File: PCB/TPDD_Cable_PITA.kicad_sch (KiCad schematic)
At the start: 5 parts

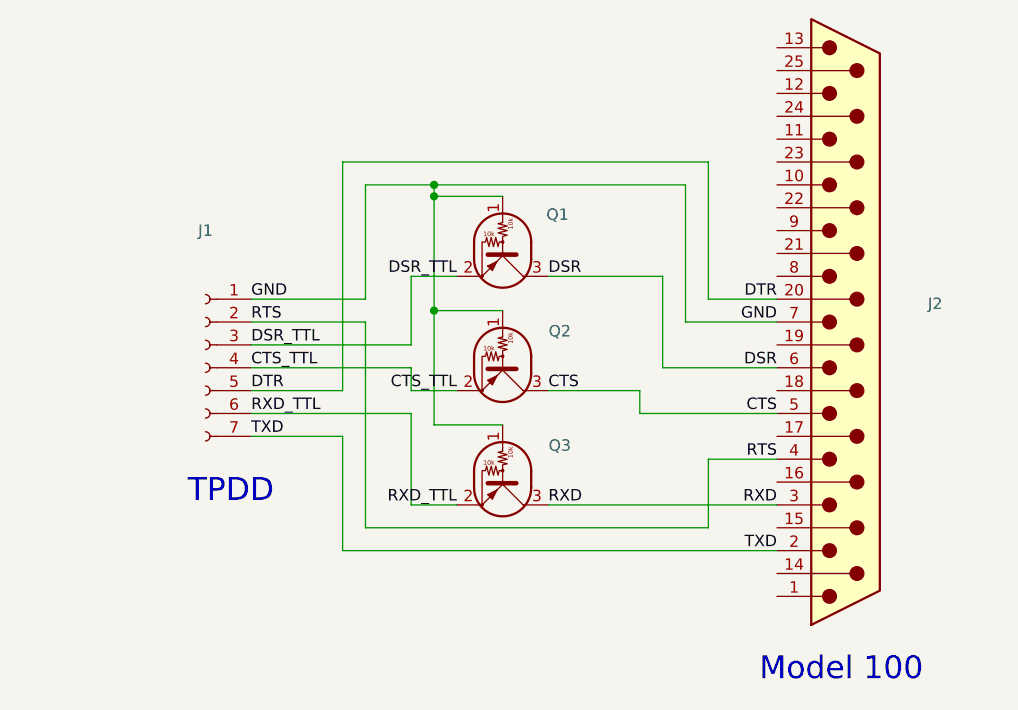
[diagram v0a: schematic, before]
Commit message: 3d printed plug housing
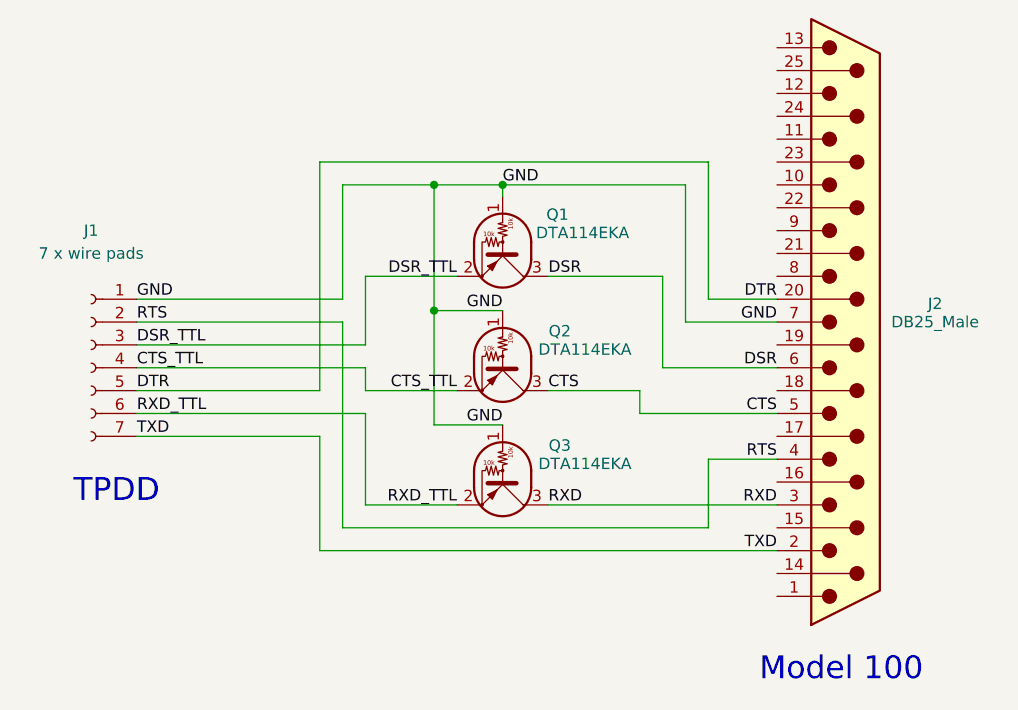
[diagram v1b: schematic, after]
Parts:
- J1: value (none) -> 7 x wire pads; footprint (none) -> 000_LOCAL:pins_1x7_2mm
- J2: value (none) -> DB25_Male; footprint (none) -> 000_LOCAL:DSUB-25_Male_EdgeMount_P2.77mm
- Q1, Q2, Q3: value (none) -> DTA114EKA; footprint (none) -> 000_LOCAL:SC-59
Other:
- moved on the sheet: J1
